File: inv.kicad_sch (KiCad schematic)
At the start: 1 part, among them U4 74LS04

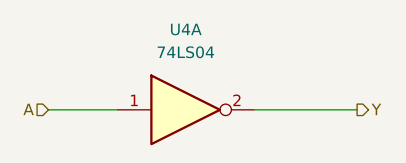
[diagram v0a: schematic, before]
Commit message: WIP - Updated code to work in separate phases:
-Read schematics into classes
-Generate netlists - working!
-Write verilog files (still needs to write pins properly)
Also:
-added verilog library with NOT and NOR2 symbols
-added parsing of each page, even the top one, in case you want a design with a single page
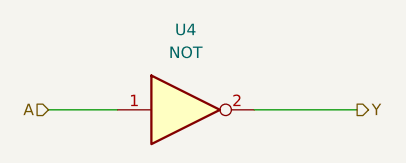
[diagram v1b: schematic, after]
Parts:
- removed U4: 74LS04, symbol 74xx:74LS04
- added U4: NOT, symbol VerilogLibrary:NOT
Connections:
- net A: now also U4.1
- net Y: now also U4.2
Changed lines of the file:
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@@
     (effects (font (size 1.27 1.27)) (justify right))
   )
-  (symbol (lib_id "74xx:74LS04") (at 78.74 44.45 0)
+  (symbol (lib_id "VerilogLibrary:NOT") (at 78.74 44.45 0)
     (in_bom yes) (on_board yes) (fields_autoplaced)
     (property "Reference" "U4" (id 0) (at 78.74 35.56 0))
-    (property "Value" "74LS04" (id 1) (at 78.74 38.1 0))
+    (property "Value" "NOT" (id 1) (at 78.74 38.1 0))
     (property "Footprint" "" (id 2) (at 78.74 44.45 0)
       (effects (font (size 1.27 1.27)) hide)
     )
-    (property "Datasheet" "http://www.ti.com/lit/gpn/sn74LS04" (id 3) (at 78.74 44.45 0)
+    (property "Datasheet" "" (id 3) (at 78.74 44.45 0)
       (effects (font (size 1.27 1.27)) hide)
     )
